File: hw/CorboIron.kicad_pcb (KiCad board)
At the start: 2 copper layers, 158.8 x 99.1 mm, 97 parts, among them P1 CONN_01X03, P10 CONN_01X04, P11 CONN_01X04, P2 CONN_01X03, P3 CONN_01X03, P4 Arduino_nano, P5 CONN_01X03, P6 CONN_01X04, P7 CONN_01X02, P8 CONN_01X03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

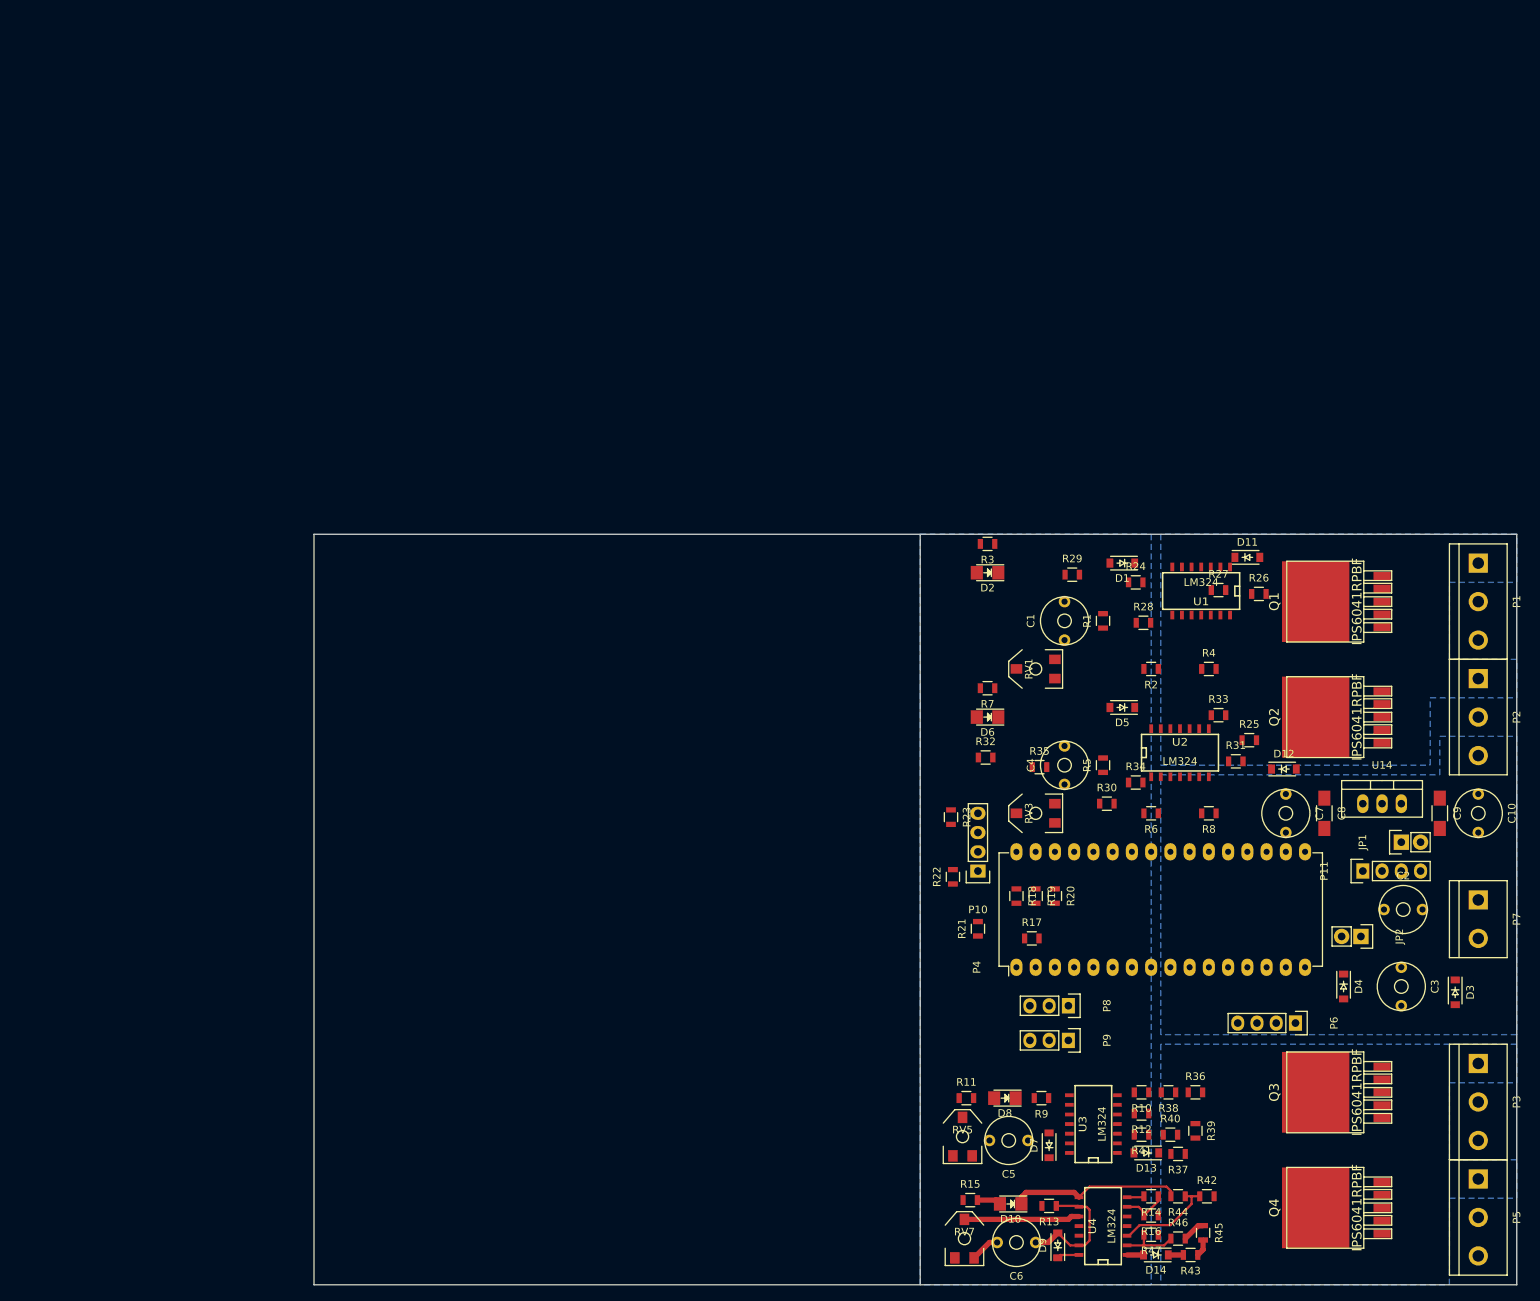
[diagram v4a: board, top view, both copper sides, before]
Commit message: Completely routed but not pretty or functional, need wider traces for the heater currents!
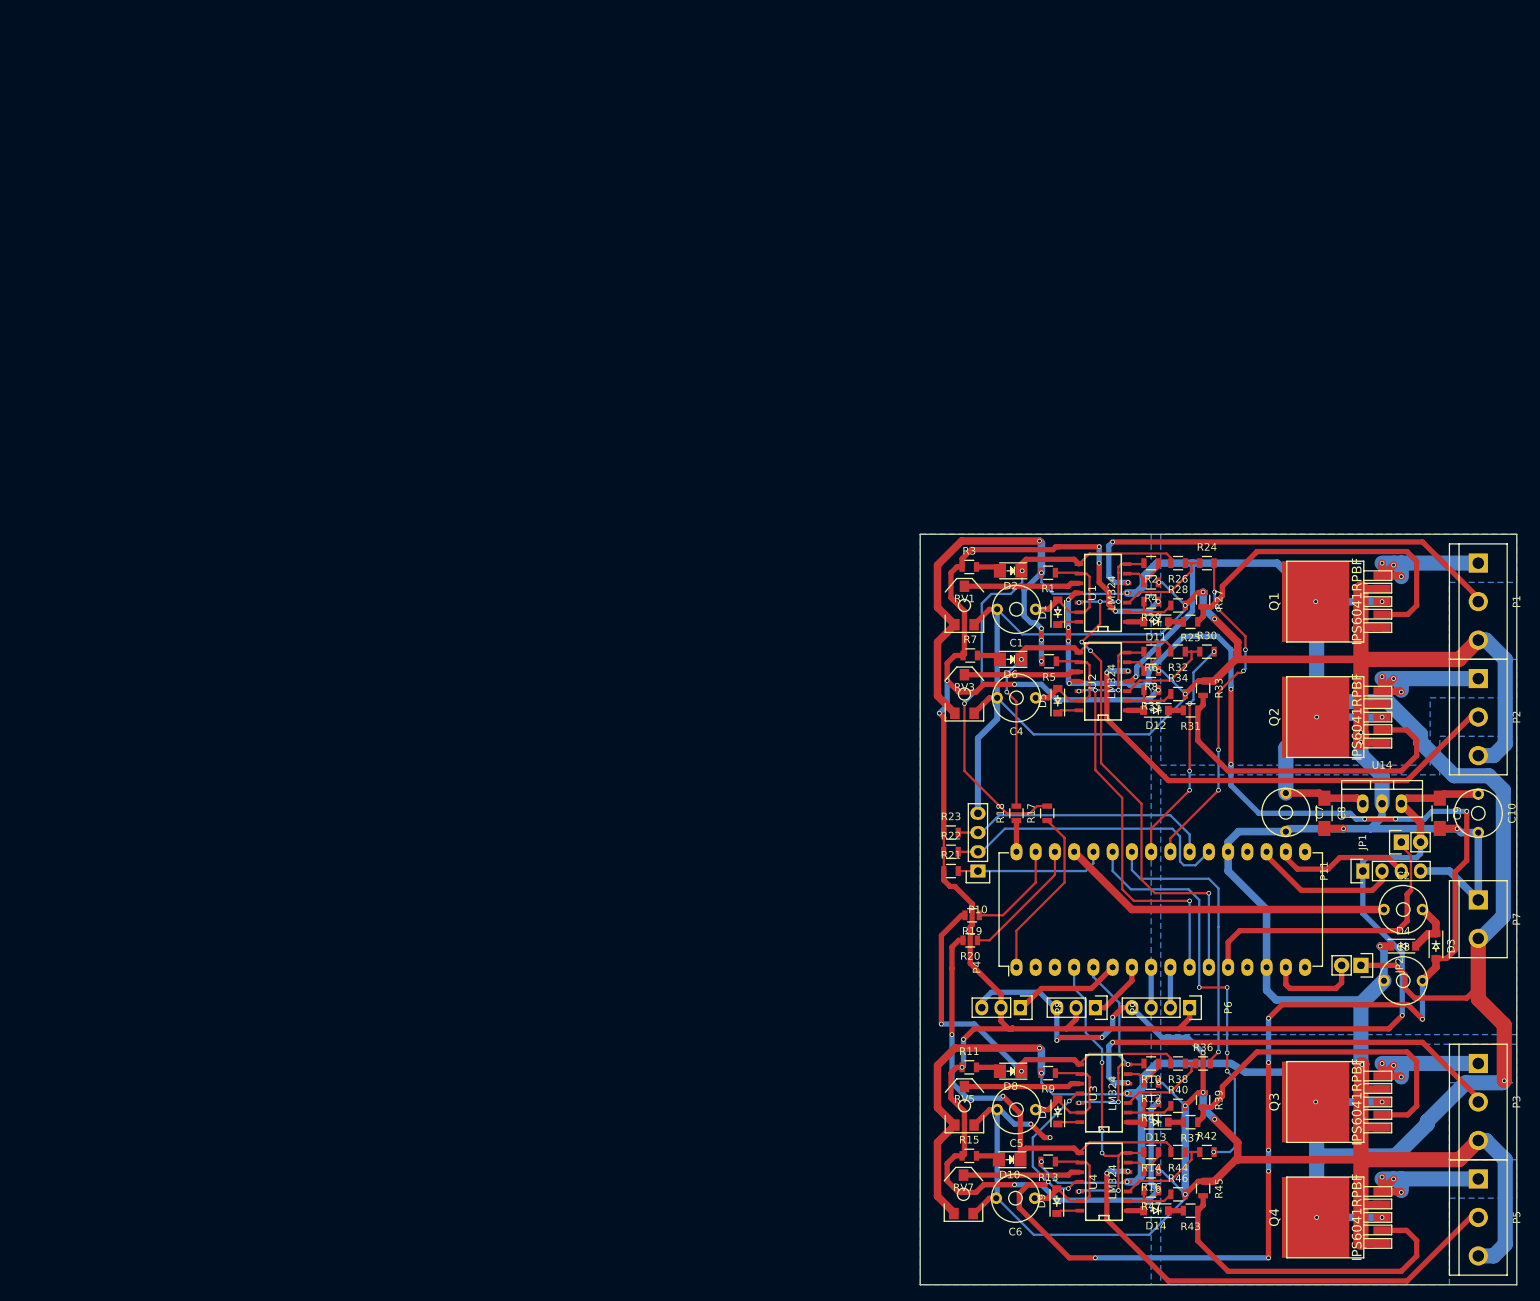
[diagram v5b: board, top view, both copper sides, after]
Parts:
- moved R32 29.0 mm to (150.9, 80.3), turned to 180 degrees
- moved R30 24.0 mm to (154.7, 80.3)
- moved R6 21.3 mm to (147.3, 80.3)
- moved R8 20.3 mm to (147.3, 82.8)
- moved D12 18.6 mm to (148.0, 88.0), turned to 180 degrees
- moved RV3 18.3 mm to (122.7, 85.9), turned to 0 degrees
- moved R35 17.9 mm to (147.3, 85.3), turned to 180 degrees
- moved R25 17.4 mm to (152.5, 76.3), turned to 180 degrees
- moved R17 16.6 mm to (133.6, 101.6), turned to 90 degrees
- moved R5 15.5 mm to (133.9, 81.5), turned to 180 degrees
- moved D11 14.8 mm to (148.0, 76.3), turned to 180 degrees
- moved P6 14.1 mm to (152.4, 127.3)
- moved R2 14.0 mm to (147.3, 68.6)
- moved U2 13.8 mm to (140.8, 84.2), turned to 90 degrees
- moved R4 13.7 mm to (147.3, 71.1), turned to 180 degrees
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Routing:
- net GND: track 6.95 -> 576.2 mm, vias 0 -> 27
- net +12V: track 0.00 -> 444.4 mm, vias 0 -> 21
- net +5V: track 0.00 -> 315.1 mm, vias 0 -> 14
- net /V_NEG: track 0.00 -> 237.8 mm, vias 0 -> 19
- net /TEMP3_AMP: track 0.00 -> 73.8 mm, vias 0 -> 6
- net /TEMP3_OK: track 0.00 -> 67.5 mm, vias 0 -> 2
- net /TEMP0: track 0.00 -> 65.0 mm, vias 0 -> 2
- net /TEMP2: track 0.00 -> 65.0 mm, vias 0 -> 2
- net /TEMP1: track 0.00 -> 59.6 mm, vias 0 -> 2
- net /TEMP3: track 0.00 -> 59.6 mm, vias 0 -> 2
- net /TEMP2_AMP: track 0.00 -> 59.4 mm, vias 0 -> 4
- net /HTR0_EN: track 0.00 -> 55.4 mm, vias 0 -> 5
- net /TEMP1_OK: track 0.00 -> 51.7 mm, vias 0 -> 2
- net Net-(Q1-Pad2): track 0.00 -> 45.7 mm
- net Net-(Q3-Pad2): track 0.00 -> 45.7 mm
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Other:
- board size 158.8 x 99.1 mm -> 78.7 x 99.1 mm

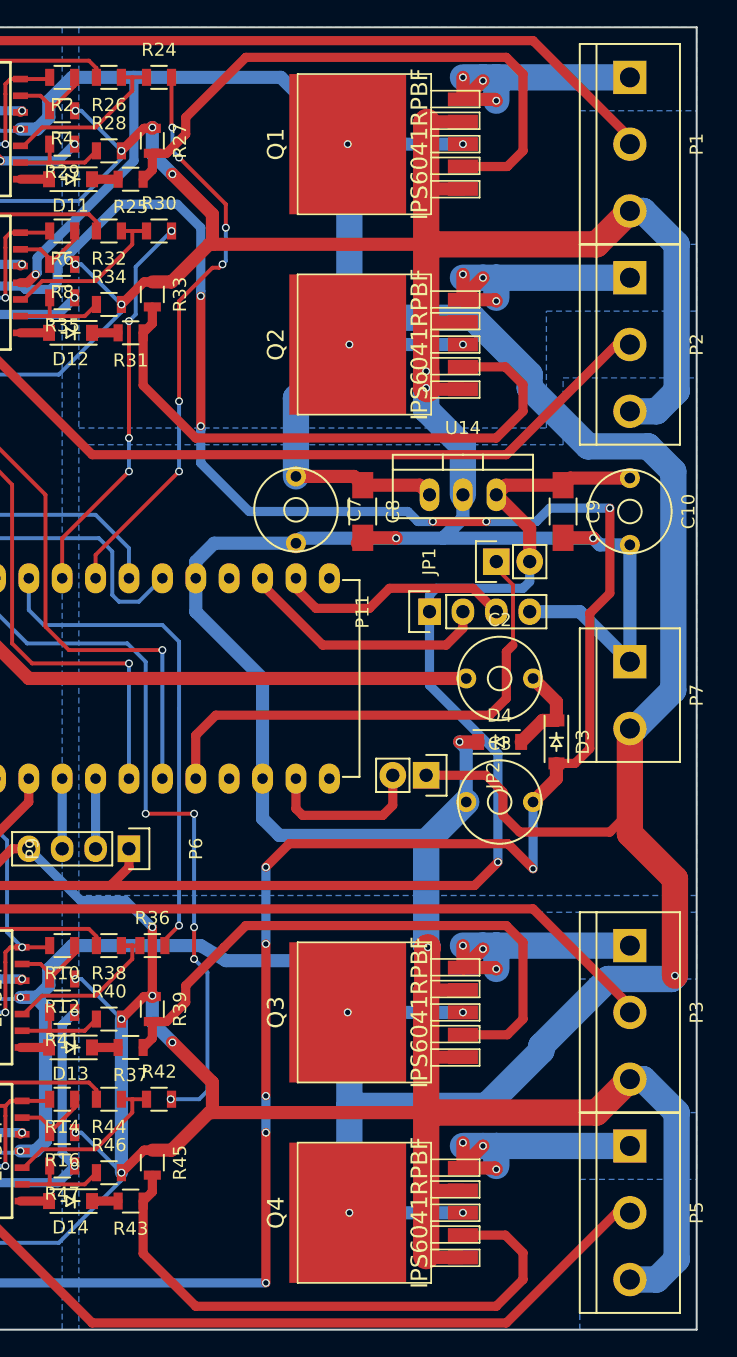
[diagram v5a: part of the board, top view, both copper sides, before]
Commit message: Some via stitching
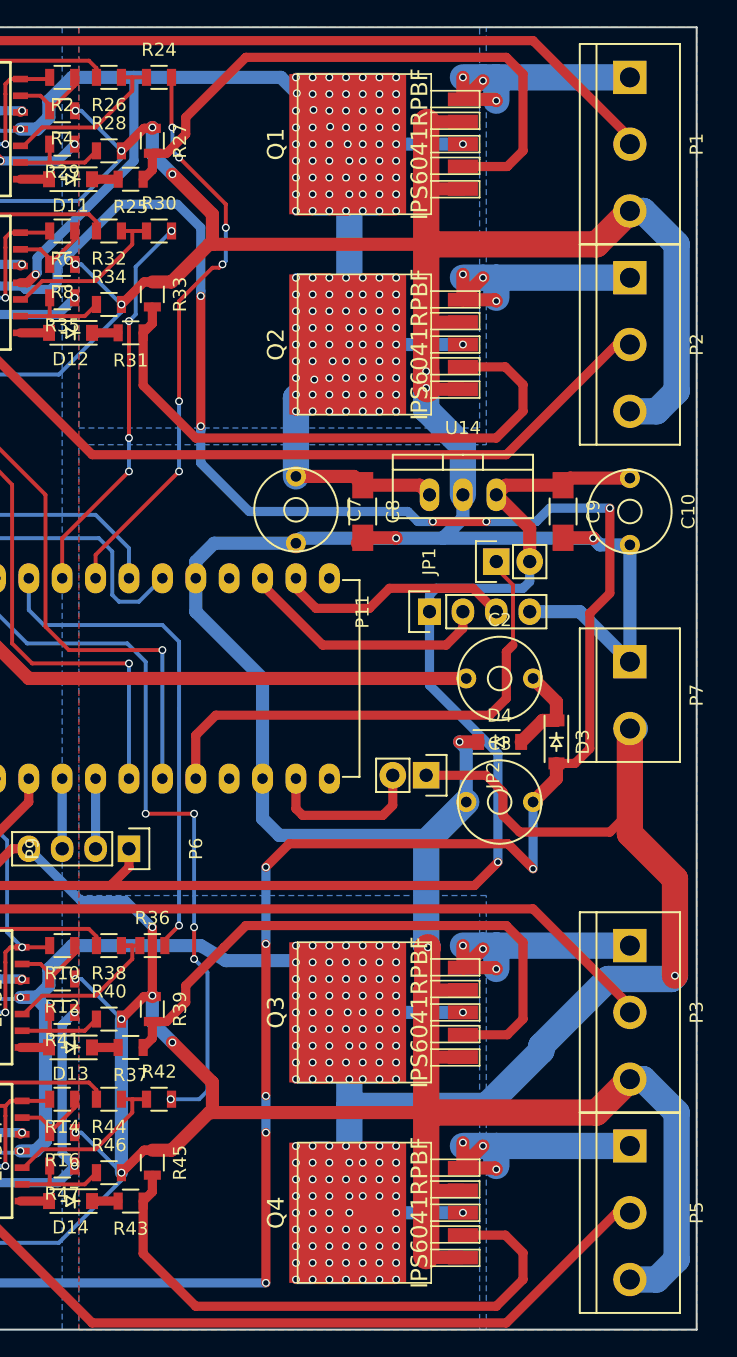
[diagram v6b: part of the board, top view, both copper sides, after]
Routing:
- net +12V: track 444.4 -> 743.1 mm, vias 21 -> 267
- added copper zone on F.Cu, net +12V

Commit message: perhaps usable
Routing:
- net GND: track 576.2 -> 425.3 mm, vias 27 -> 34
- net +12V: track 743.1 -> 770.7 mm, vias 267 -> 266

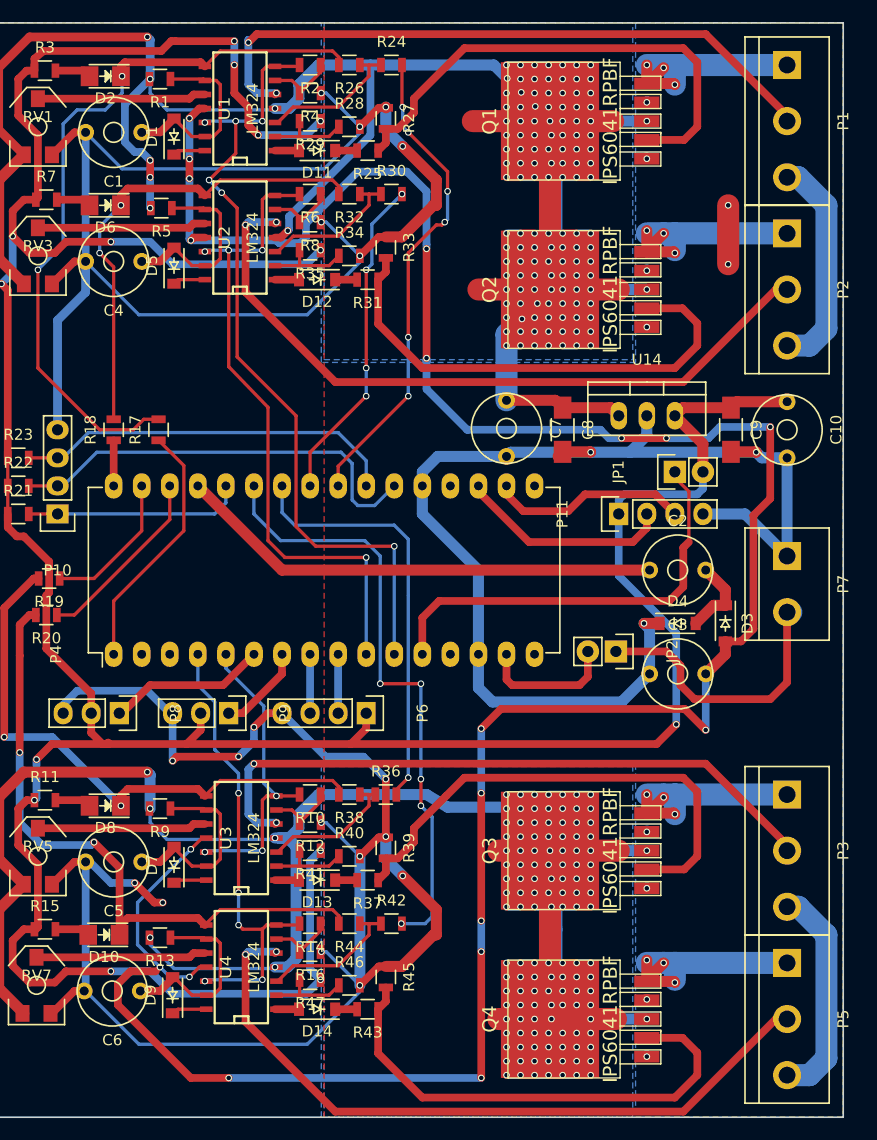
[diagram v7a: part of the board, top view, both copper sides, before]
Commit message: Added pulldown resistors for opamp logic started placeing refdes and values on silkscreen
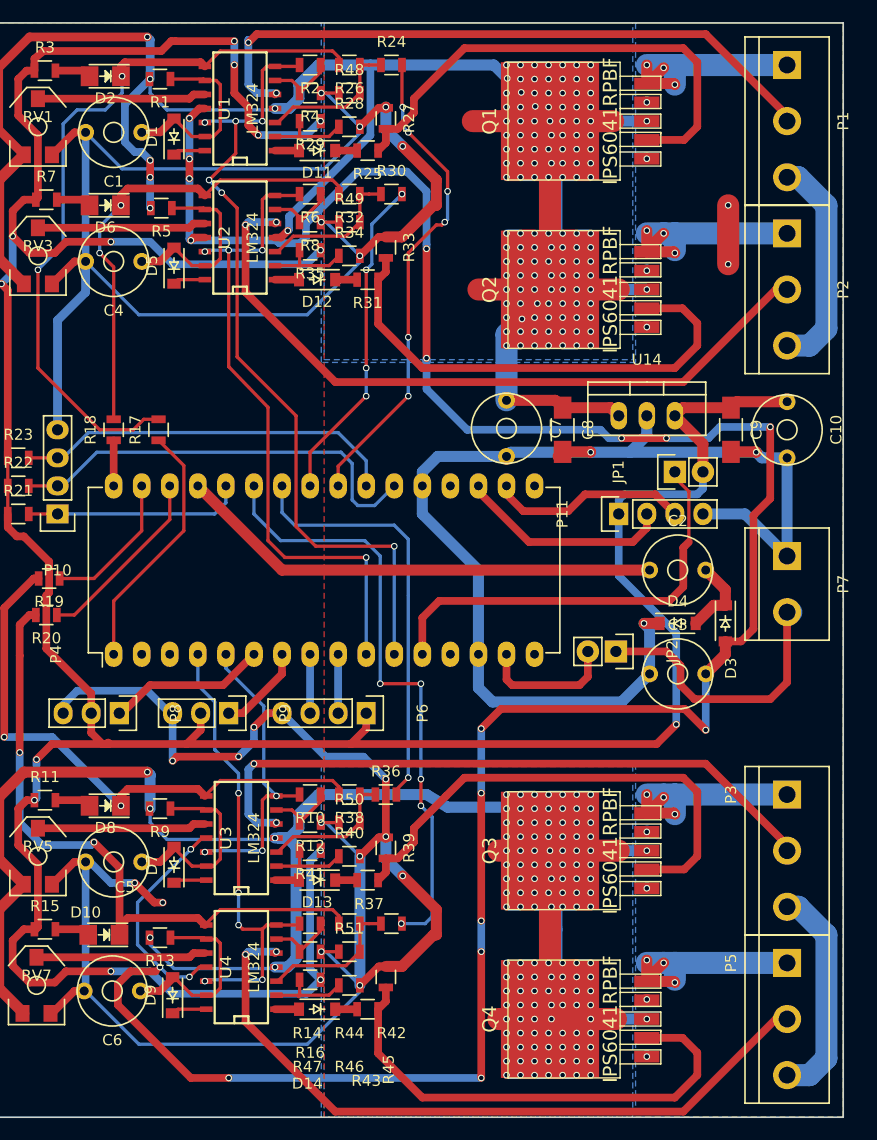
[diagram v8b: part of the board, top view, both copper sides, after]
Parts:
- added R48: 27K, Resistors_SMD:R_0805, F.Cu at (150.9, 71.1)
- added R49: 27K, Resistors_SMD:R_0805, F.Cu at (150.9, 82.8)
- added R50: 27K, Resistors_SMD:R_0805, F.Cu at (150.9, 137.2)
- added R51: 27K, Resistors_SMD:R_0805, F.Cu at (150.9, 148.8)
- C1, C4, C5, C6: value CP1 -> 1uF
- C10, C7: value CP1 -> 100u
- C2: value CP1 -> 4u7
- C3: value CP1 -> 220u
- C8, C9: value C -> 10n
- R1, R13, R17, R18, R19, R20, R21, R22, R23, R5, R9: value R -> 100K
- R10, R14, R2, R6: value R -> 680K
- R11, R15, R34, R35, R40, R41, R46, R47, R7: value R -> 4K7
- R12, R16, R4, R8: value R -> 1K
- R24, R30, R36, R42: value R -> 22K
- R25, R31, R37, R43: value R -> 6K8
- R26, R32, R38, R44: value R -> 150K
- R27, R33, R39, R45: value R -> 2K7
- R28, R29, R3: value R -> 4k7
- RV1, RV3, RV5, RV7: value POT -> 5K
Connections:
- P4 pad 13: (no net) -> Net-(P4-Pad13)
- P4 pad 16: (no net) -> Net-(P4-Pad16)
- P4 pad 17: (no net) -> Net-(P4-Pad17)
- P4 pad 2: (no net) -> +3V3
- P4 pad 20: (no net) -> Net-(P4-Pad20)
- P4 pad 3: (no net) -> /REF
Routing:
- net (no net): track 0.00 -> 5.33 mm, vias 0 -> 2
- net GND: track 425.3 -> 426.6 mm, vias 34 -> 32
